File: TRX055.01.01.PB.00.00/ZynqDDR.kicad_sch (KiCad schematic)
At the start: 3 parts, among them U1 XC7Z015-1CLG485I, U2 AS4C256M16D3, U3 AS4C256M16D3

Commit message: Update Layout
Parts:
- U1: footprint XC7Z015:CLG485XC7Z012S&slash_XC7Z015_AMD -> CLG485XC7Z012S/XC7Z015_AMD; JLCPCB Part # (none) -> C1522056
- U2, U3: value AS4C256M16D3 -> K4B4G1646E-BYMA; JLCPCB Part # (none) -> C500275
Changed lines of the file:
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@@
 			)
 		)
-		(property "Value" "AS4C256M16D3"
+		(property "Value" "K4B4G1646E-BYMA"
 			(at 309.626 241.808 0)
 			(effects
@@
 		)
 		(property "Description" "4Gb (256Mx16 bit) Double Data Rate 3 Synchronous DRAM"
+			(at 303.53 196.85 0)
+			(effects
+				(font
+					(size 1.27 1.27)
+				)
+				(hide yes)
+			)
+		)
+		(property "JLCPCB Part #" "C500275"
 			(at 303.53 196.85 0)
 			(effects
@@
 			)
 		)
-		(property "Value" "AS4C256M16D3"
+		(property "Value" "K4B4G1646E-BYMA"
 			(at 306.832 129.54 0)
 			(effects
@@
 		)
 		(property "Description" "4Gb (256Mx16 bit) Double Data Rate 3 Synchronous DRAM"
+			(at 306.07 87.63 0)
+			(effects
+				(font
+					(size 1.27 1.27)
+				)
+				(hide yes)
+			)
+		)
+		(property "JLCPCB Part #" "C500275"
 			(at 306.07 87.63 0)
 			(effects
@@
 	)
 	(symbol
-		(lib_name "XC7Z015-1CLG485I_2")
 		(lib_id "XC7Z015-1CLG485C:XC7Z015-1CLG485I")
 		(at 100.33 91.44 0)
@@
 			)
 		)
-		(property "Footprint" "XC7Z015:CLG485XC7Z012S&slash_XC7Z015_AMD"
+		(property "Footprint" "CLG485XC7Z012S/XC7Z015_AMD"
 			(at 100.33 91.44 0)
 			(effects
@@
 			(at 100.33 91.44 0)
 			(effects
+				(font
+					(size 1.27 1.27)
+				)
+				(hide yes)
+			)
+		)
+		(property "JLCPCB Part #" "C1522056"
+			(at 100.33 91.44 0)
+			(effects

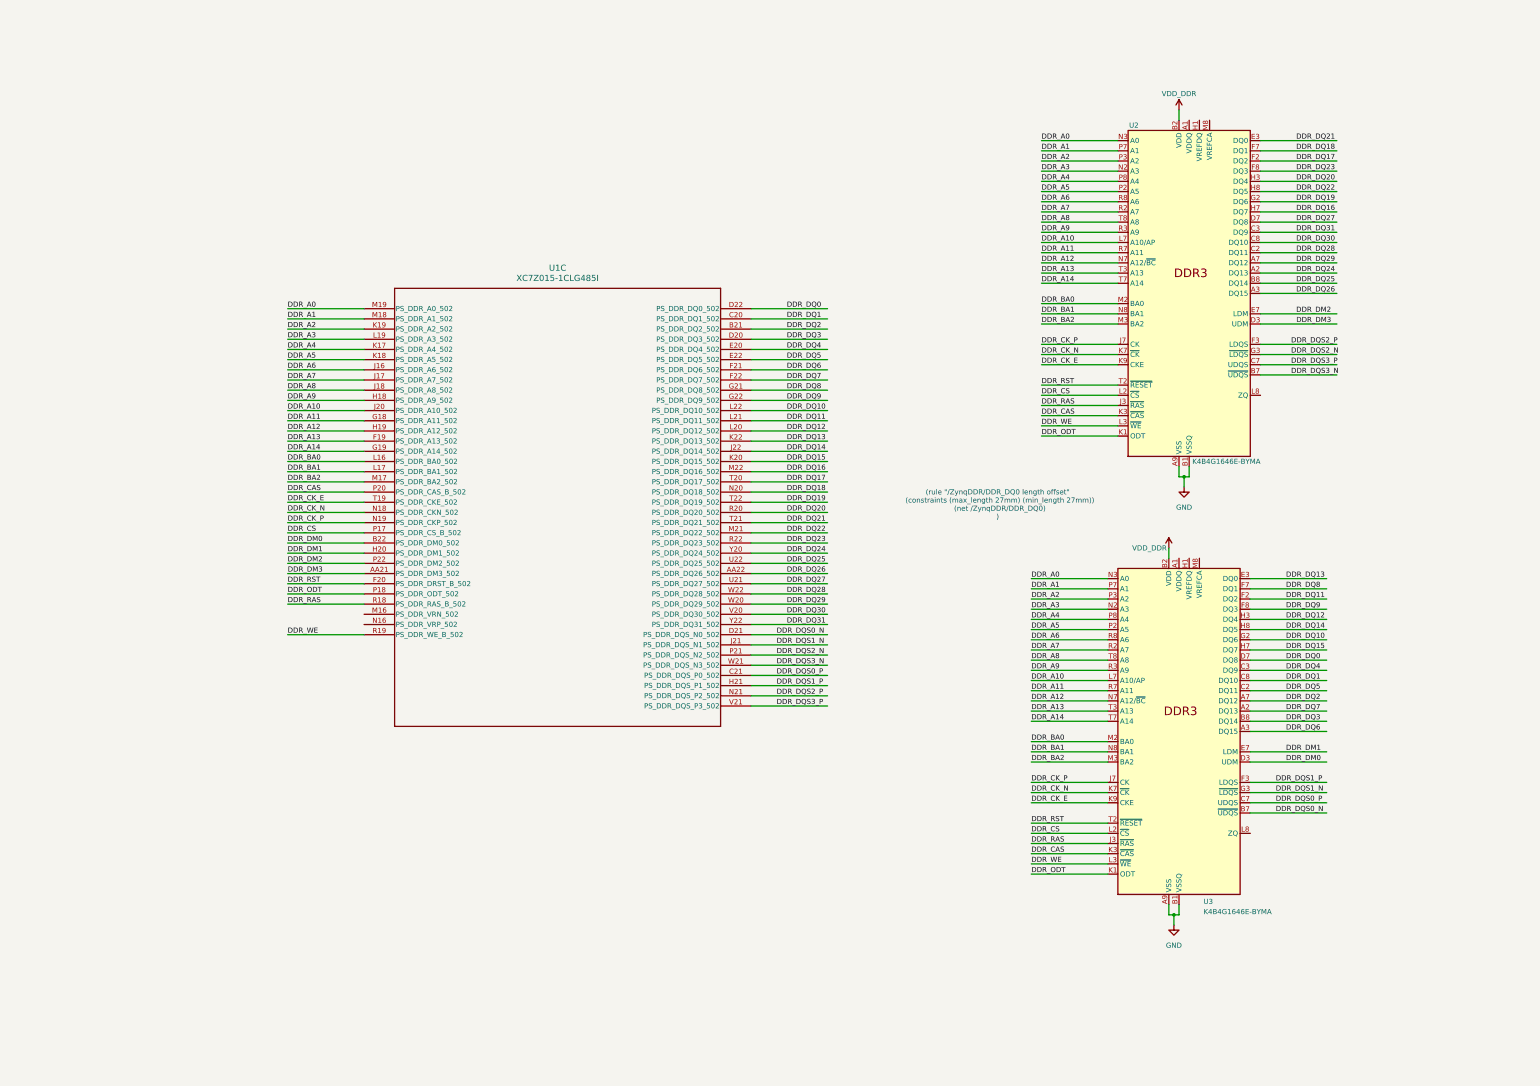
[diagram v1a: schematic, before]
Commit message: +ETH +USB +Connectors
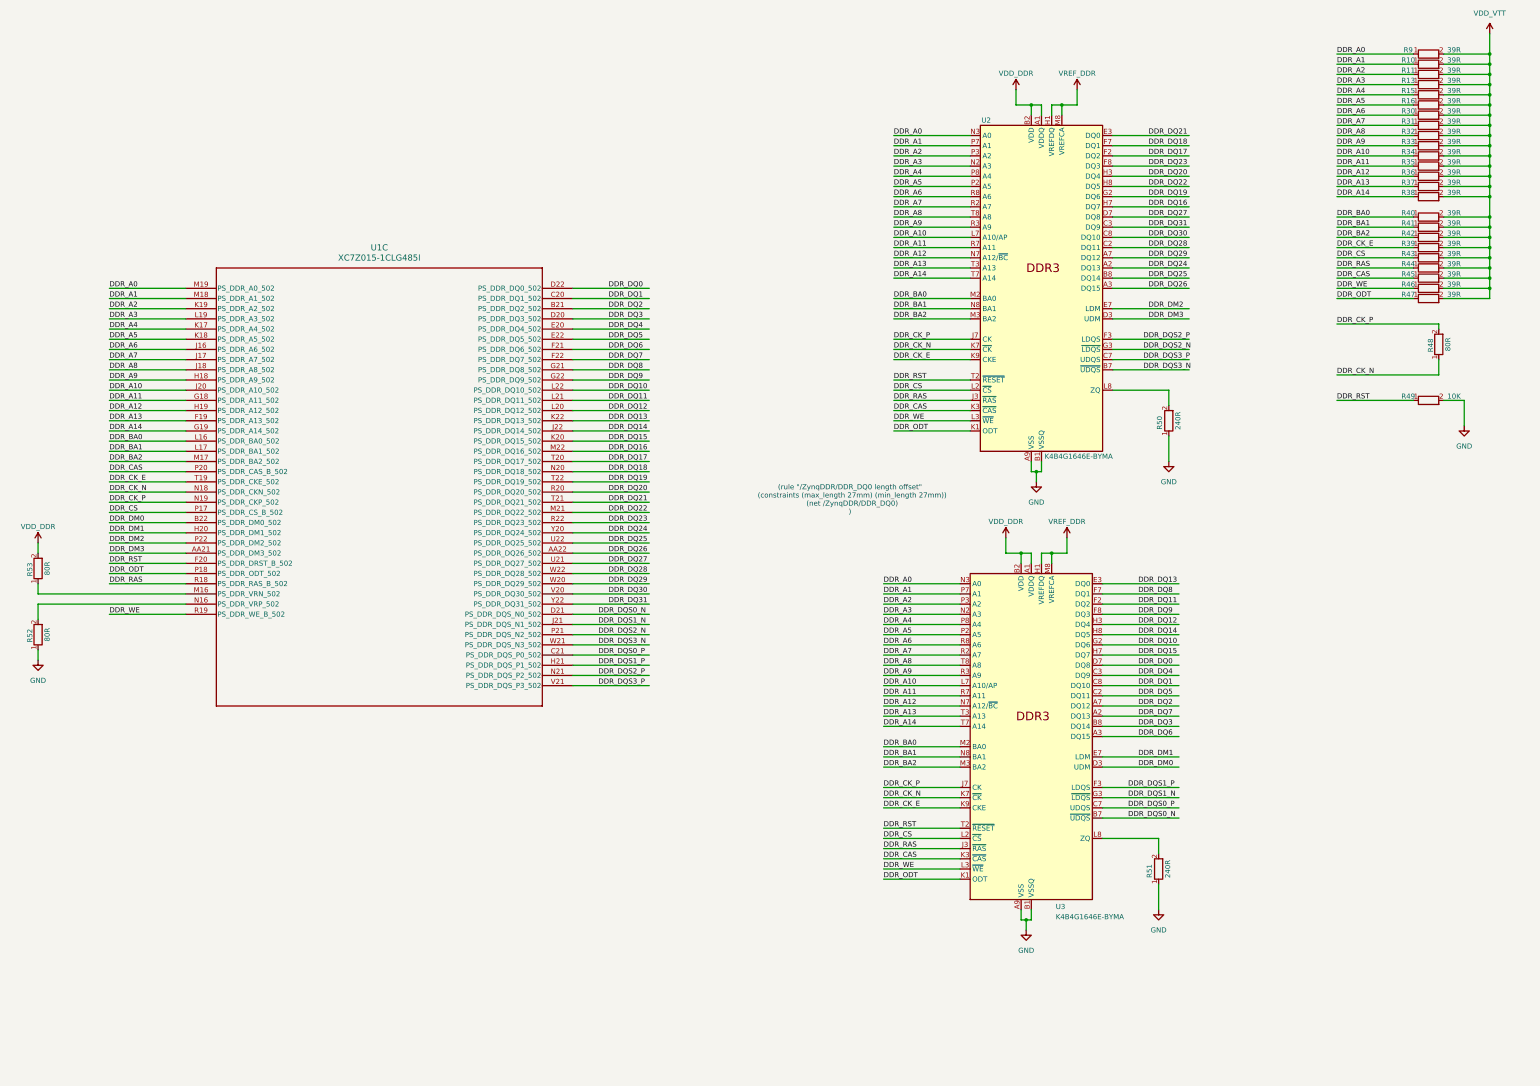
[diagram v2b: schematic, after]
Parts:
- added R10, R11, R13, R15, R16, R30, R31, R32, R33, R34, R35, R36, R37, R38, R39, R40, R41, R42, R43, R44, R45, R46, R47, R9: 39R, Resistor_SMD:R_0402_1005Metric, symbol PPA-Pasive:Res
- added R48, R52, R53: 80R, Resistor_SMD:R_0402_1005Metric, symbol PPA-Pasive:Res
- added R49: 10K, Resistor_SMD:R_0402_1005Metric, symbol PPA-Pasive:Res
- added R50, R51: 240R, Resistor_SMD:R_0402_1005Metric, symbol PPA-Pasive:Res
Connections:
- net DDR_A0: now also R9.1
- net DDR_A1: now also R10.1
- net DDR_A10: now also R34.1
- net DDR_A11: now also R35.1
- net DDR_A12: now also R36.1
- net DDR_A13: now also R37.1
- net DDR_A14: now also R38.1
- net DDR_A2: now also R11.1
- net DDR_A3: now also R13.1
- net DDR_A4: now also R15.1
- net DDR_A5: now also R16.1
- net DDR_A6: now also R30.1
- net DDR_A7: now also R31.1
- net DDR_A8: now also R32.1
- net DDR_A9: now also R33.1
- net DDR_BA0: now also R40.1
- net DDR_BA1: now also R41.1
- net DDR_BA2: now also R42.1
- net DDR_CAS: now also R45.1
- net DDR_CK_E: now also R39.1
- net DDR_CK_N: now also R48.1
- net DDR_CK_P: now also R48.2
- net DDR_CS: now also R43.1
- net DDR_ODT: now also R47.1
- net DDR_RAS: now also R44.1
- net DDR_RST: now also R49.1
- net DDR_WE: now also R46.1
- net GND: now also R49.2, R50.1, R51.1, R52.1
- net VDD_DDR: now also U2.A1 (VDDQ), U2.A8 (VDDQ), U2.C1 (VDDQ), U2.C9 (VDDQ), U2.D2 (VDDQ), U2.E9 (VDDQ), U2.F1 (VDDQ), U2.H2 (VDDQ), U2.H9 (VDDQ), U3.A1 (VDDQ), U3.A8 (VDDQ), U3.C1 (VDDQ), U3.C9 (VDDQ), U3.D2 (VDDQ), U3.E9 (VDDQ), U3.F1 (VDDQ), U3.H2 (VDDQ), U3.H9 (VDDQ), R53.2
- net VREF_DDR: now reaches U3.H1 (VREFDQ)
- net VREF_DDR: now also U2.H1 (VREFDQ), U2.M8 (VREFCA), U3.M8 (VREFCA)
- net at U3.L8 (ZQ): now also R51.2
- net at U2.L8 (ZQ): now also R50.2
- net at U1.M16 (PS_DDR_VRN_502): now also R53.1
- net at U1.N16 (PS_DDR_VRP_502): now also R52.2
- new net VDD_VTT: R10.2, R11.2, R13.2, R15.2, R16.2, R30.2, R31.2, R32.2, R33.2, R34.2, R35.2, R36.2, R37.2, R38.2, R39.2, R40.2, R41.2, R42.2, R43.2, R44.2, R45.2, R46.2, R47.2, R9.2
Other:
- moved on the sheet: U1C, U2, U3

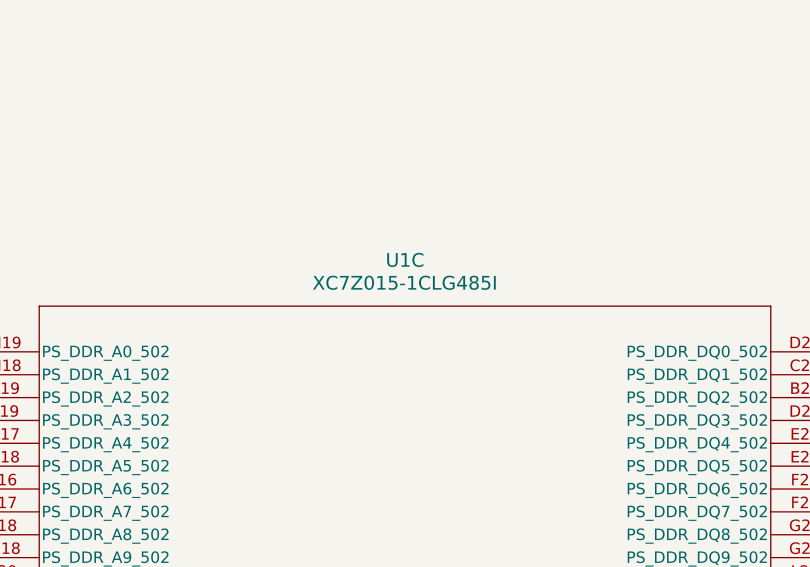
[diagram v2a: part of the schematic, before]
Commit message: + add clocks + add PSU
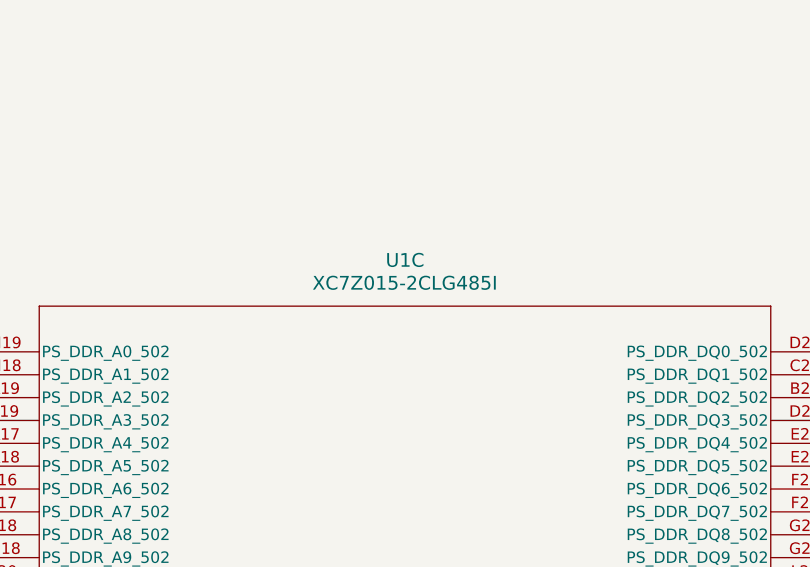
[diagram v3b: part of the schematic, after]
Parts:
- R10, R11, R13, R15, R16, R30, R31, R32, R33, R34, R35, R36, R37, R38, R39, R40, R41, R42, R43, R44, R45, R46, R47, R9: JLCPCB Part # (none) -> C25110
- R48, R52, R53: JLCPCB Part # (none) -> C854436
- R49: JLCPCB Part # (none) -> C25744
- R50, R51: JLCPCB Part # (none) -> C25153
- U1: value XC7Z015-1CLG485I -> XC7Z015-2CLG485I; JLCPCB Part # C1522056 -> C1522056

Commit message: V0.1 - production, added brig-up comments
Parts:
- added C327, C328, C329, C330, C331, C332, C333, C334, C335, C336, C337, C338, C339, C340, C341, C342, C343, C344, C345, C346, C347, C348, C349, C350, C351, C352, C353, C354, C355, C356, C357, C358, C359, C360, C361, C362, C363, C364, C365, C366, C367, C368: M1, Capacitor_SMD:C_0201_0603Metric, symbol PPA-Pasive:Cap
- added C378, C379, C380, C381: 100M, Capacitor_SMD:C_1206_3216Metric, symbol PPA-Pasive:Cap
- U1: footprint CLG485XC7Z012S/XC7Z015_AMD -> XC7Z015:CLG485XC7Z012S&slash_XC7Z015_AMD
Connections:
- net DDR_A0: now also R41.1; no longer R9.1
- net DDR_A1: now also R35.1; no longer R10.1
- net DDR_A10: now also R10.1; no longer R34.1
- net DDR_A11: now also R31.1; no longer R35.1
- net DDR_A12: now also R13.1; no longer R36.1
- net DDR_A13: now also R32.1; no longer R37.1
- net DDR_A14: now also R34.1; no longer R38.1
- net DDR_A3: now also R40.1; no longer R13.1
- net DDR_A4: now also R36.1; no longer R15.1
- net DDR_A5: now also R33.1; no longer R16.1
- net DDR_A7: now also R38.1; no longer R31.1
- net DDR_A8: now also R16.1; no longer R32.1
- net DDR_A9: now also R37.1; no longer R33.1
- net DDR_BA0: now also R39.1; no longer R40.1
- net DDR_BA1: now also R15.1; no longer R41.1
- net DDR_BA2: now also R47.1; no longer R42.1
- net DDR_CAS: now also R9.1; no longer R45.1
- net DDR_CK_E: now also R42.1; no longer R39.1
- net DDR_CS: now also R44.1; no longer R43.1
- net DDR_ODT: now also R46.1; no longer R47.1
- net DDR_RAS: now also R43.1; no longer R44.1
- net DDR_WE: now also R45.1; no longer R46.1
- net GND: now also C327.2, C328.2, C329.2, C330.2, C331.2, C332.2, C333.2, C334.2, C335.2, C336.2, C337.2, C338.2, C339.2, C340.2, C341.2, C342.2, C343.2, C344.2, C345.2, C346.2, C347.2, C348.2, C349.2, C350.2, C351.2, C352.2, C353.2, C354.2, C355.2, C356.2, C357.2, C358.2, C359.2, C360.2, C361.2, C362.2, C363.2, C364.2, C365.2, C366.2, C367.2, C368.2, C378.2, C379.2, C380.2, C381.2
- net VDD_DDR: now also C331.1, C332.1, C333.1, C334.1, C335.1, C336.1, C337.1, C338.1, C339.1, C340.1, C341.1, C342.1, C343.1, C344.1, C345.1, C346.1, C347.1, C348.1, C349.1, C350.1, C351.1, C352.1, C353.1, C354.1, C355.1, C356.1, C357.1, C358.1, C359.1, C360.1, C361.1, C362.1, C363.1, C364.1, C365.1, C366.1, C367.1, C368.1, C378.1, C379.1, C380.1, C381.1
- net VREF_DDR: now also C327.1, C328.1, C329.1, C330.1
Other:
- company: (none) -> Tronex s.r.o. / Tronex Group USA LLC
- title: (none) -> TRNX SDR Carrier board
